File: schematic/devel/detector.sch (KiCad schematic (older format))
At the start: 16 parts

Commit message: separated symbol library according to functionality
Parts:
- D?: symbol common:S599x -> Sensor_OpticalPosition:S599x
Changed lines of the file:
@@
 $EndDescr
 $Comp
-L common:S599x D?
+L Sensor_OpticalPosition:S599x D?
 U 1 1 5D92E8C4
 P 4750 3950

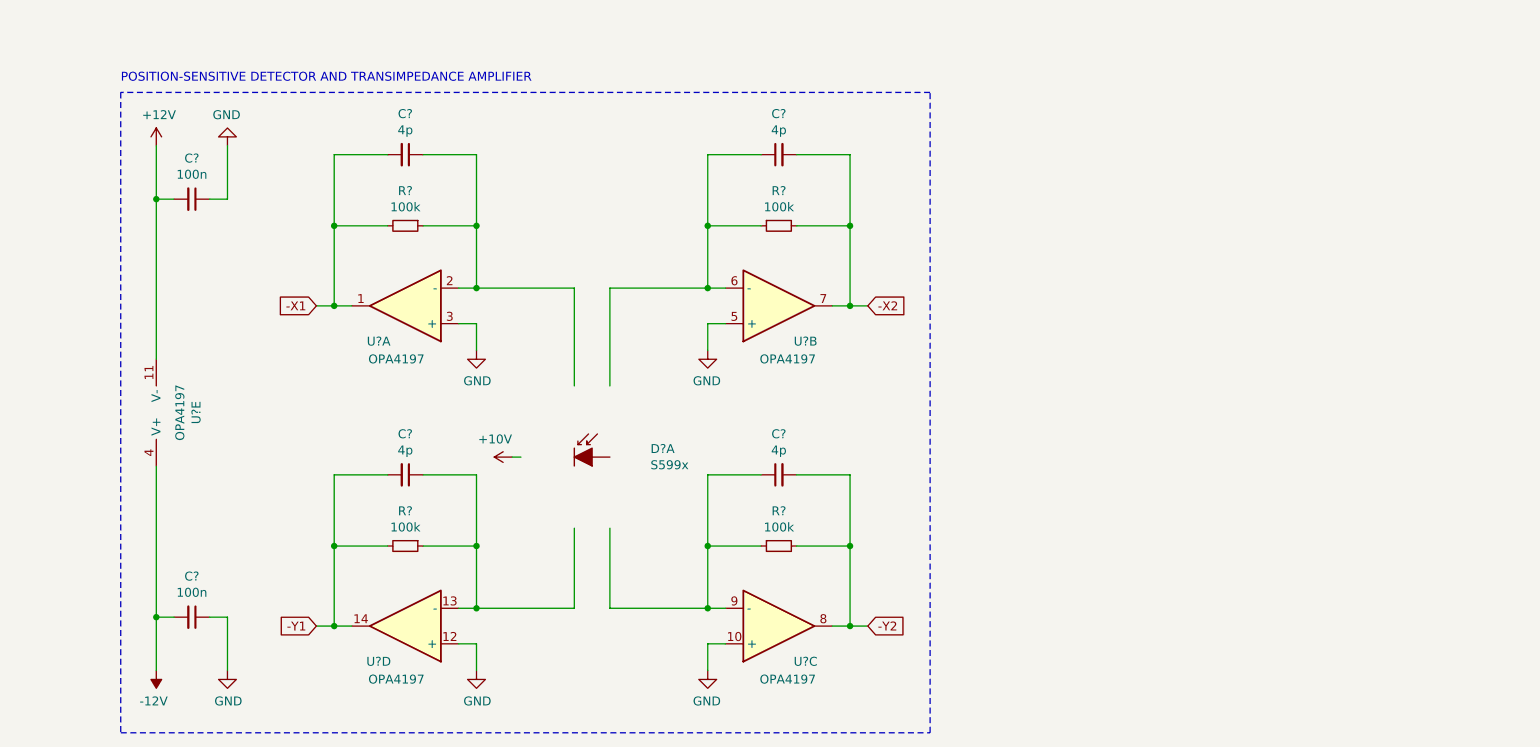
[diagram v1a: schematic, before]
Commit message: redesigned S599x symbol according to symbol guidelines
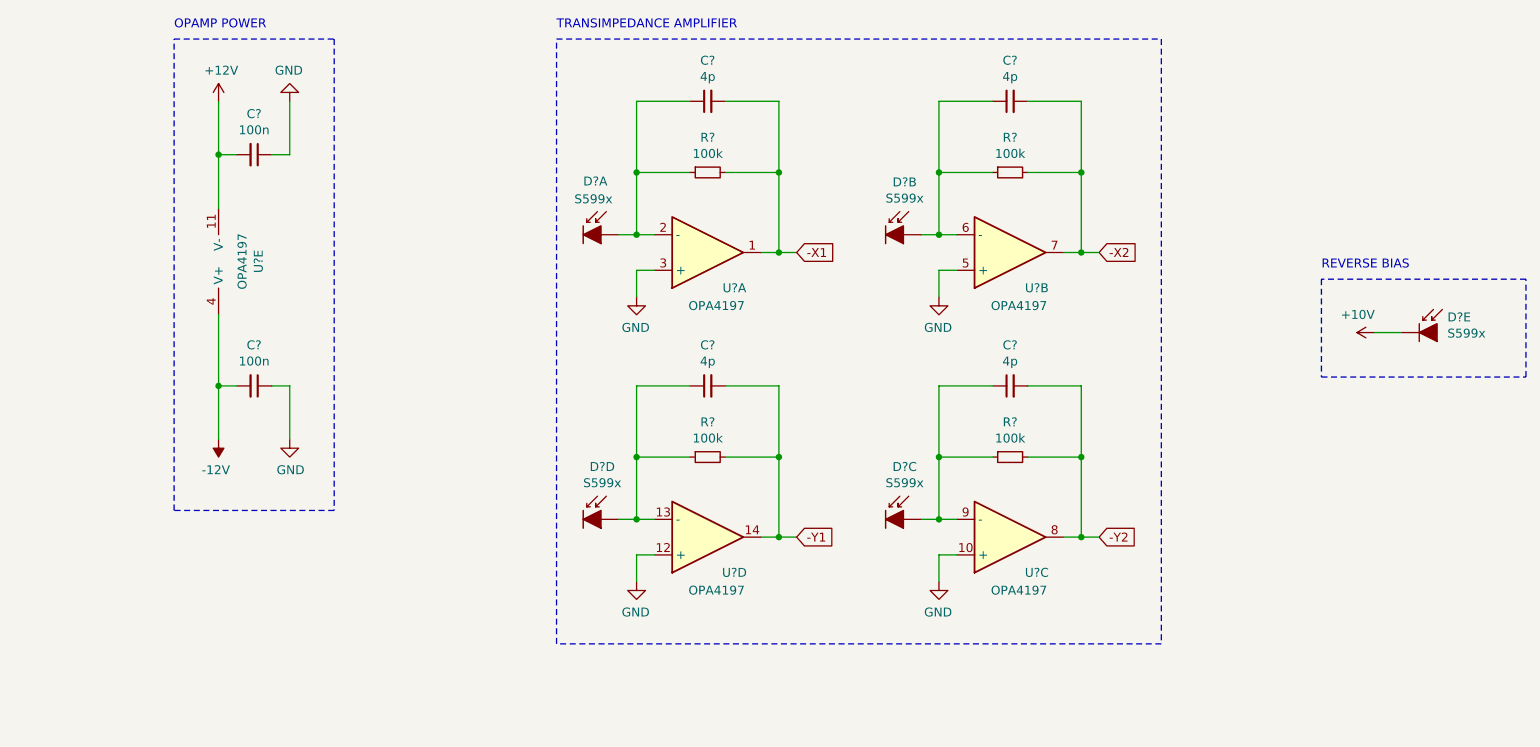
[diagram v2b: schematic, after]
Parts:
- added D? (x4): S599x, symbol Sensor_OpticalPosition:S599x
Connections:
- wire segments 71 -> 67
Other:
- note added: "OPAMP POWER"
- note added: "REVERSE BIAS"
- note added: "TRANSIMPEDANCE AMPLIFIER"
- note removed: "POSITION-SENSITIVE DETECTOR AND TRANSIMPEDANCE AMPLIFIER"
- moved on the sheet: C?, D?A, R?, U?A, U?B, U?C, U?D, U?E

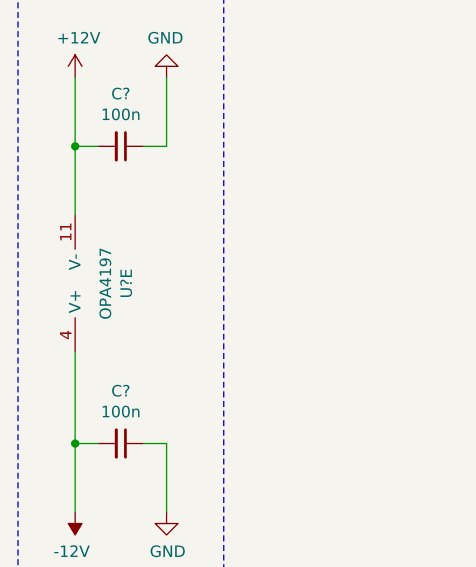
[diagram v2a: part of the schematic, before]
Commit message: fixed opamp supply voltage polarisation, fixed output buffers
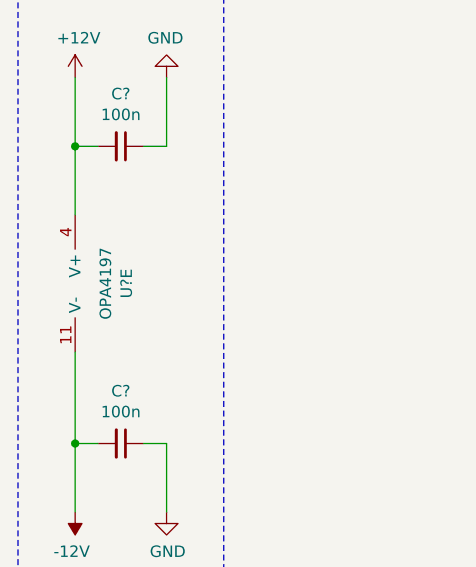
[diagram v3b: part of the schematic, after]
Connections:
- net +12V: now also U?.4 (V+); no longer U?.11 (V-)
- net -12V: now also U?.11 (V-); no longer U?.4 (V+)
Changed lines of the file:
@@
 F 3 "~" H 2550 2850 50  0001 C CNN
 	5    2550 2850
-	-1   0    0    1
+	-1   0    0    -1
 $EndComp
 Wire Wire Line

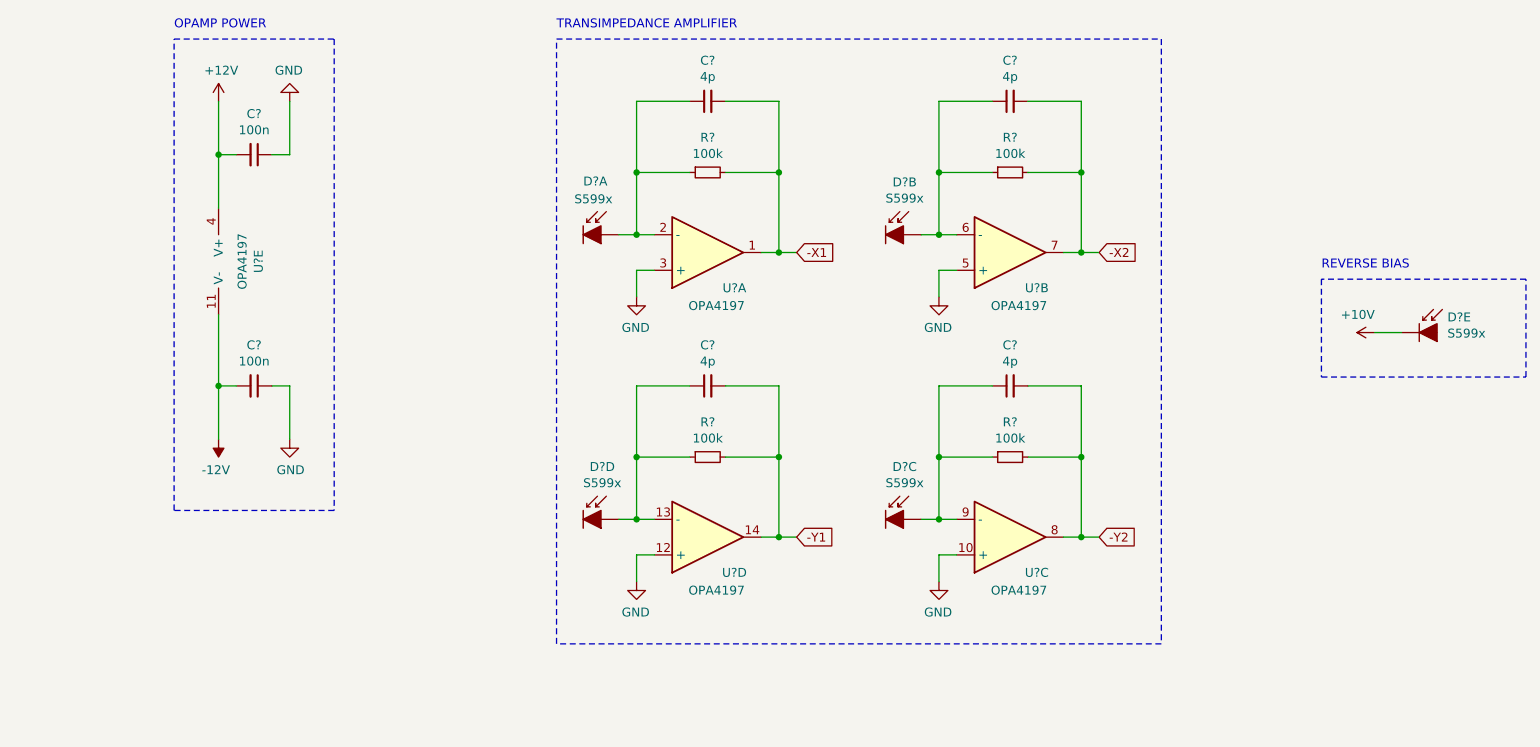
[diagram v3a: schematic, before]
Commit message: fixed floating buffer in arthimetic unit
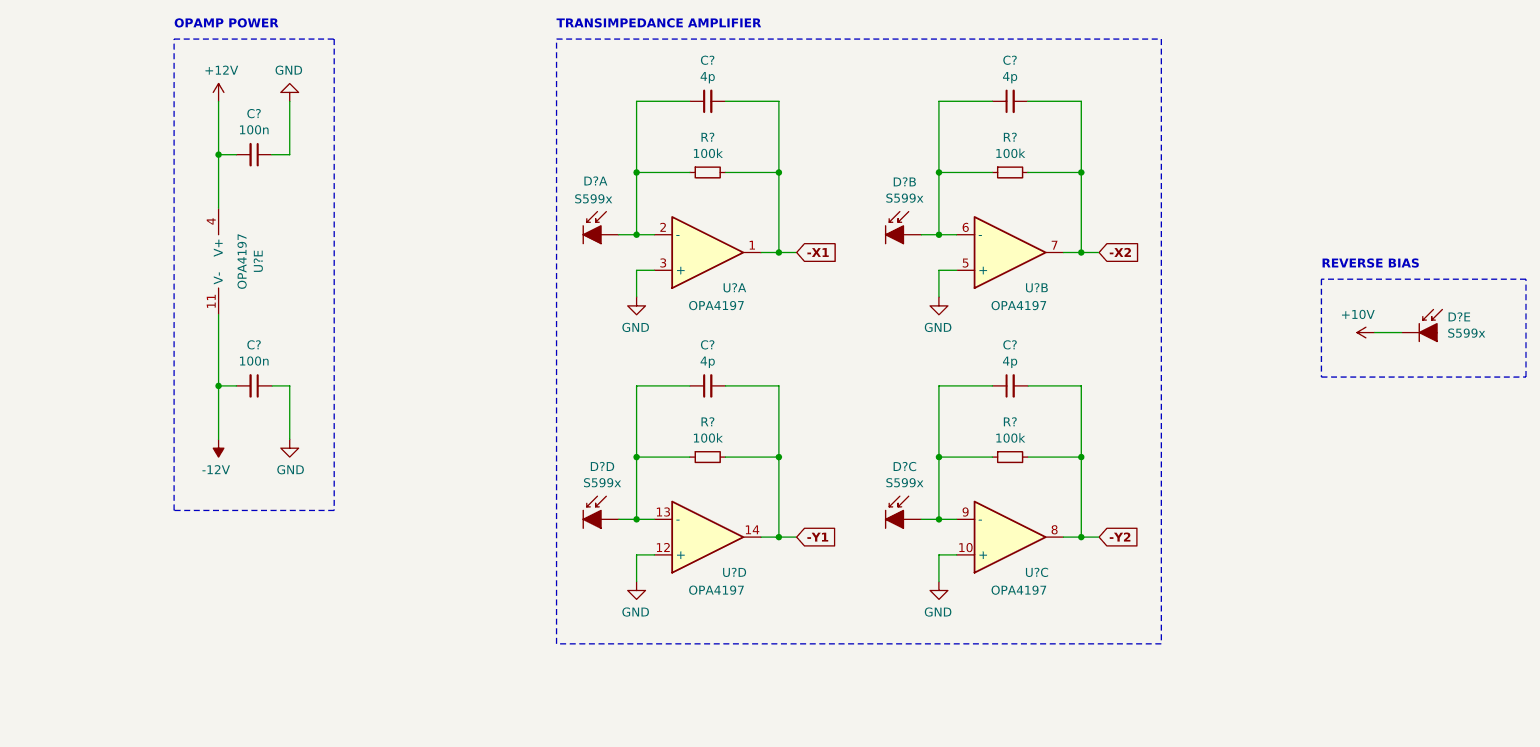
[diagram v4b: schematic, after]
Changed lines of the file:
@@
 P 6700 3050
 AR Path="/5D92E8E8" Ref="#PWR?"  Part="1"
-AR Path="/5D929D0E/5D92E8E8" Ref="#PWR?"  Part="1"
-F 0 "#PWR?" H 6700 2800 50  0001 C CNN
+AR Path="/5D929D0E/5D92E8E8" Ref="#PWR0153"  Part="1"
+F 0 "#PWR0153" H 6700 2800 50  0001 C CNN
 F 1 "GND" H 6705 2877 50  0000 C CNN
 F 2 "" H 6700 3050 50  0001 C CNN
@@
 P 6700 4650
 AR Path="/5D92E913" Ref="#PWR?"  Part="1"
-AR Path="/5D929D0E/5D92E913" Ref="#PWR?"  Part="1"
-F 0 "#PWR?" H 6700 4400 50  0001 C CNN
+AR Path="/5D929D0E/5D92E913" Ref="#PWR0154"  Part="1"
+F 0 "#PWR0154" H 6700 4400 50  0001 C CNN
 F 1 "GND" H 6705 4477 50  0000 C CNN
 F 2 "" H 6700 4650 50  0001 C CNN
@@
 	-1   0    0    -1
 $EndComp
-Text GLabel 7600 4400 2    50   Input ~ 0
+Text GLabel 7600 4400 2    50   Input ~ 6
 -Y2
 Wire Wire Line
 	7600 4400 7500 4400
 Connection ~ 7500 4400
-Text GLabel 7600 2800 2    50   Input ~ 0
+Text GLabel 7600 2800 2    50   Input ~ 6
 -X2
 $Comp
@@
 Wire Wire Line
 	5900 2800 5800 2800
-Text GLabel 5900 2800 2    50   Input ~ 0
+Text GLabel 5900 2800 2    50   Input ~ 6
 -X1
 $Comp
@@
 P 5000 3050
 AR Path="/5D92E928" Ref="#PWR?"  Part="1"
-AR Path="/5D929D0E/5D92E928" Ref="#PWR?"  Part="1"
-F 0 "#PWR?" H 5000 2800 50  0001 C CNN
+AR Path="/5D929D0E/5D92E928" Ref="#PWR0155"  Part="1"
+F 0 "#PWR0155" H 5000 2800 50  0001 C CNN
 F 1 "GND" H 5005 2877 50  0000 C CNN
 F 2 "" H 5000 3050 50  0001 C CNN
@@
 Wire Wire Line
 	5900 4400 5800 4400
-Text GLabel 5900 4400 2    50   Input ~ 0
+Text GLabel 5900 4400 2    50   Input ~ 6
 -Y1
 $Comp
@@
 P 5000 4650
 AR Path="/5D92E959" Ref="#PWR?"  Part="1"
-AR Path="/5D929D0E/5D92E959" Ref="#PWR?"  Part="1"
-F 0 "#PWR?" H 5000 4400 50  0001 C CNN
+AR Path="/5D929D0E/5D92E959" Ref="#PWR0156"  Part="1"
+F 0 "#PWR0156" H 5000 4400 50  0001 C CNN
 F 1 "GND" H 5005 4477 50  0000 C CNN
 F 2 "" H 5000 4650 50  0001 C CNN
@@
 P 9150 3250
 AR Path="/5D92E97A" Ref="#PWR?"  Part="1"
-AR Path="/5D929D0E/5D92E97A" Ref="#PWR?"  Part="1"
-F 0 "#PWR?" H 9150 3100 50  0001 C CNN
+AR Path="/5D929D0E/5D92E97A" Ref="#PWR0157"  Part="1"
+F 0 "#PWR0157" H 9150 3100 50  0001 C CNN
 F 1 "+10V" V 9250 3250 50  0000 L CNN
 F 2 "" H 9150 3250 50  0001 C CNN
@@
 P 3050 1950
 AR Path="/5D92E99E" Ref="#PWR?"  Part="1"
-AR Path="/5D929D0E/5D92E99E" Ref="#PWR?"  Part="1"
-F 0 "#PWR?" H 3050 1700 50  0001 C CNN
+AR Path="/5D929D0E/5D92E99E" Ref="#PWR0158"  Part="1"
+F 0 "#PWR0158" H 3050 1700 50  0001 C CNN
 F 1 "GND" H 3055 1777 50  0000 C CNN
 F 2 "" H 3050 1950 50  0001 C CNN
@@
 P 2650 1950
 AR Path="/5D92E9A4" Ref="#PWR?"  Part="1"
-AR Path="/5D929D0E/5D92E9A4" Ref="#PWR?"  Part="1"
-F 0 "#PWR?" H 2650 1800 50  0001 C CNN
+AR Path="/5D929D0E/5D92E9A4" Ref="#PWR0159"  Part="1"
+F 0 "#PWR0159" H 2650 1800 50  0001 C CNN
 F 1 "+12V" H 2665 2123 50  0000 C CNN
 F 2 "" H 2650 1950 50  0001 C CNN
@@
 P 3050 3850
 AR Path="/5D92E9B0" Ref="#PWR?"  Part="1"
-AR Path="/5D929D0E/5D92E9B0" Ref="#PWR?"  Part="1"
-F 0 "#PWR?" H 3050 3600 50  0001 C CNN
+AR Path="/5D929D0E/5D92E9B0" Ref="#PWR0160"  Part="1"
+F 0 "#PWR0160" H 3050 3600 50  0001 C CNN
 F 1 "GND" H 3055 3677 50  0000 C CNN
 F 2 "" H 3050 3850 50  0001 C CNN
@@
 P 2650 3850
 AR Path="/5D92E9B6" Ref="#PWR?"  Part="1"
-AR Path="/5D929D0E/5D92E9B6" Ref="#PWR?"  Part="1"
-F 0 "#PWR?" H 2650 3950 50  0001 C CNN
+AR Path="/5D929D0E/5D92E9B6" Ref="#PWR0161"  Part="1"
+F 0 "#PWR0161" H 2650 3950 50  0001 C CNN
 F 1 "-12V" H 2665 4023 50  0000 C CNN
 F 2 "" H 2650 3850 50  0001 C CNN
@@
 Wire Notes Line
 	4550 1600 7950 1600
-Text Notes 4550 1550 0    50   ~ 0
+Text Notes 4550 1550 0    50   ~ 6
 TRANSIMPEDANCE AMPLIFIER
 $Comp
@@
 Wire Notes Line
 	10000 2950 8850 2950
-Text Notes 8850 2900 0    50   ~ 0
+Text Notes 8850 2900 0    50   ~ 6
 REVERSE BIAS
 Wire Notes Line
@@
 Wire Notes Line
 	2400 4250 2400 1600
-Text Notes 2400 1550 0    50   ~ 0
+Text Notes 2400 1550 0    50   ~ 6
 OPAMP POWER
 $EndSCHEMATC

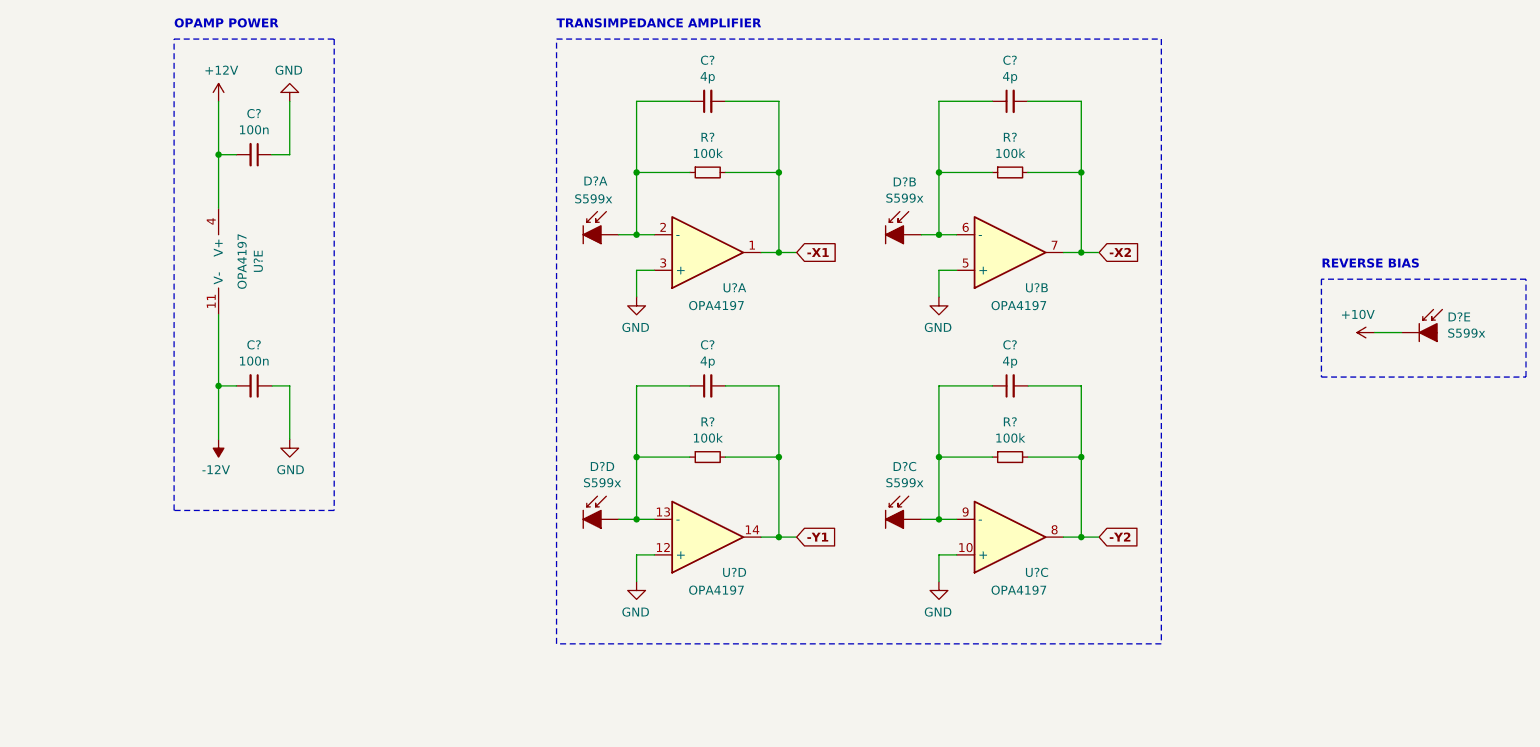
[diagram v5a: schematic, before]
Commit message: removed arithmetic unit from development board, changed output connectors
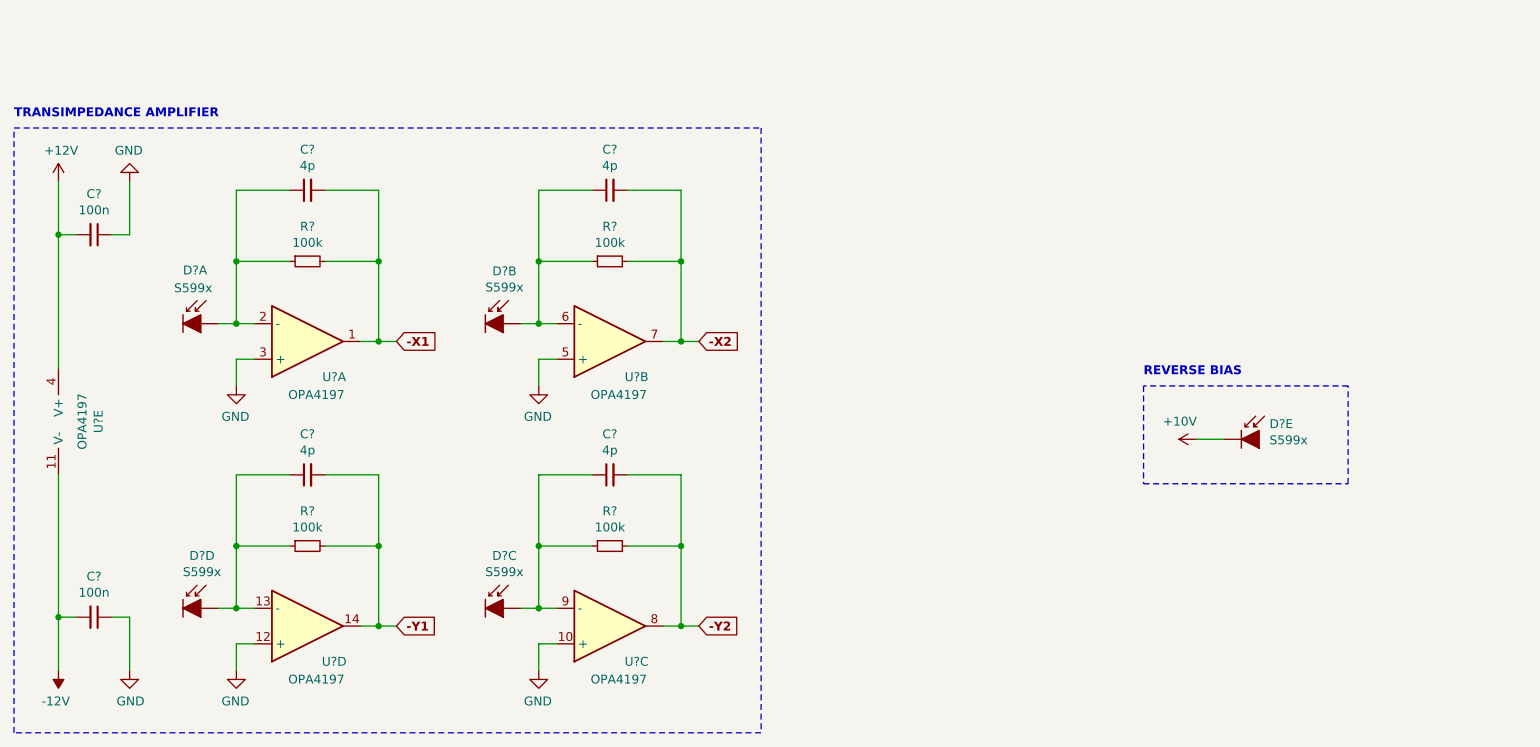
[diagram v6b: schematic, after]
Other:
- note removed: "OPAMP POWER"
- moved on the sheet: C?, D?A, D?B, D?C, D?D, D?E, R?, U?A, U?B, U?C, U?D, U?E
